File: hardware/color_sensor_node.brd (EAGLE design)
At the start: 27.9 x 27.9 mm, 20 parts, among them J1 JTAG, J2 JTAG, U1 ISL29125, U2 3.3V, U3 WS2811

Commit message: idk
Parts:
- D1: device SparkFun-LED:WS2812B -> SparkFun-LED:WS2812-2020
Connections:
- net 5V: now also D1.4; no longer D1.1
- net DOUT: now also D1.1; no longer D1.2
- net GND: now also D1.2; no longer D1.3
- net N$4: now also D1.3; no longer D1.4
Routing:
- net 5V: track 27.7 -> 31.3 mm
- net DOUT: track 1.54 -> 4.05 mm
- net GND: track 16.5 -> 19.0 mm
- net N$4: track 10.7 -> 12.9 mm
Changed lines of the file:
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@@
 <attribute name="VALUE" x="3.302" y="19.05" size="0.6096" layer="27" font="vector" ratio="20" rot="R90" align="top-center"/>
 </element>
-<element name="D1" library="SparkFun-LED" package="WS2812B" value="WS2812B" x="13.97" y="13.97" rot="R180">
-<attribute name="PROD_ID" value="DIO-12503" x="13.97" y="13.97" size="1.778" layer="27" rot="R180" display="off"/>
-<attribute name="VALUE" value="WS2812B" x="13.97" y="13.97" size="1.778" layer="27" rot="R180" display="off"/>
+<element name="D1" library="SparkFun-LED" package="WS2812-2020" value="WS2812B" x="13.97" y="13.97" rot="R180">
 <attribute name="VALUE" x="13.97" y="16.764" size="0.6096" layer="27" font="vector" ratio="20" rot="R180" align="top-center"/>
 </element>
@@
 <contactref element="U1" pad="3"/>
 <contactref element="U3" pad="4"/>
-<contactref element="D1" pad="3"/>
+<contactref element="D1" pad="2"/>
 <wire x1="7.151" y1="19.05" x2="6.6341" y2="19.05" width="0.4064" layer="1"/>
 <wire x1="8.128" y1="18.2" x2="8.001" y2="18.2" width="0.4064" layer="1"/>
@@
 <via x="19.05" y="11.43" extent="1-16" drill="0.381"/>
 <wire x1="18.33" y1="13.47" x2="16.645" y2="13.47" width="0.2032" layer="1"/>
-<wire x1="16.547" y1="13.372" x2="16.547" y2="12.37" width="0.2032" layer="1"/>
+<wire x1="16.547" y1="13.372" x2="13.055" y2="13.42" width="0.2032" layer="1"/>
 <wire x1="16.645" y1="13.47" x2="16.547" y2="13.372" width="0.2032" layer="1"/>
 <wire x1="19.05" y1="24.13" x2="21.59" y2="26.67" width="0" layer="19" extent="1-1"/>
@@
 <wire x1="18.33" y1="13.47" x2="22.18" y2="16.51" width="0" layer="19" extent="1-16"/>
 <wire x1="19.05" y1="11.43" x2="18.33" y2="13.47" width="0" layer="19" extent="1-1"/>
-<wire x1="13.97" y1="11.43" x2="16.547" y2="12.37" width="0" layer="19" extent="1-1"/>
-<wire x1="16.51" y1="8.89" x2="16.547" y2="12.37" width="0" layer="19" extent="1-1"/>
+<wire x1="13.97" y1="11.43" x2="13.055" y2="13.42" width="0" layer="19" extent="1-1"/>
+<wire x1="16.51" y1="8.89" x2="13.055" y2="13.42" width="0" layer="19" extent="1-1"/>
 <wire x1="24.13" y1="8.89" x2="24.13" y2="13.97" width="0" layer="19" extent="1-1"/>
 <wire x1="26.67" y1="6.35" x2="24.13" y2="8.89" width="0" layer="19" extent="1-1"/>
@@
 <contactref element="U2" pad="3"/>
 <contactref element="C1" pad="1"/>
-<contactref element="D1" pad="1"/>
+<contactref element="D1" pad="4"/>
 <wire x1="8.028" y1="20" x2="6.6341" y2="20" width="0.4064" layer="1"/>
 <wire x1="8.128" y1="19.9" x2="8.028" y2="20" width="0.4064" layer="1"/>
@@
 <wire x1="6.6341" y1="15.9051" x2="6.604" y2="15.875" width="0.4064" layer="1"/>
 <wire x1="6.6341" y1="18.1" x2="6.6341" y2="15.9051" width="0.4064" layer="1"/>
-<wire x1="9.957" y1="15.57" x2="11.393" y2="15.57" width="0.4064" layer="1"/>
+<wire x1="9.957" y1="15.57" x2="14.885" y2="14.52" width="0.4064" layer="1"/>
 <wire x1="9.652" y1="15.875" x2="9.957" y2="15.57" width="0.4064" layer="1"/>
 <contactref element="U3" pad="8"/>
 <via x="5.08" y="5.715" extent="1-16" drill="0.381"/>
 <wire x1="26.08" y1="13.97" x2="22.18" y2="15.24" width="0" layer="19" extent="16-16"/>
-<wire x1="11.393" y1="15.57" x2="22.18" y2="15.24" width="0" layer="19" extent="1-16"/>
+<wire x1="14.885" y1="14.52" x2="22.18" y2="15.24" width="0" layer="19" extent="1-16"/>
 <wire x1="8.3312" y1="15.875" x2="9.652" y2="15.875" width="0" layer="19" extent="1-1"/>
 <wire x1="6.6341" y1="15.9051" x2="8.3312" y2="15.875" width="0" layer="19" extent="1-1"/>
@@
 </signal>
 <signal name="DOUT">
-<contactref element="D1" pad="2"/>
+<contactref element="D1" pad="1"/>
 <contactref element="J2" pad="6"/>
-<wire x1="11.393" y1="10.832" x2="11.393" y2="12.37" width="0.4064" layer="1"/>
+<wire x1="11.393" y1="10.832" x2="13.055" y2="14.52" width="0.4064" layer="1"/>
 <via x="11.393" y="10.832" extent="1-16" drill="0.381"/>
 <wire x1="11.393" y1="10.832" x2="22.18" y2="13.97" width="0" layer="19" extent="1-16"/>
 </signal>
 <signal name="N$4">
-<contactref element="D1" pad="4"/>
+<contactref element="D1" pad="3"/>
 <contactref element="U3" pad="5"/>
 <wire x1="9.398" y1="12.065" x2="8.3312" y2="12.065" width="0.4064" layer="1"/>
 <wire x1="9.779" y1="12.446" x2="9.398" y2="12.065" width="0.4064" layer="1"/>
-<wire x1="16.547" y1="15.57" x2="16.205" y2="15.57" width="0.4064" layer="1"/>
+<wire x1="14.885" y1="13.42" x2="16.205" y2="15.57" width="0.4064" layer="1"/>
 <wire x1="15.24" y1="14.605" x2="10.16" y2="14.605" width="0.4064" layer="1"/>
 <wire x1="10.16" y1="14.605" x2="9.779" y2="14.224" width="0.4064" layer="1"/>

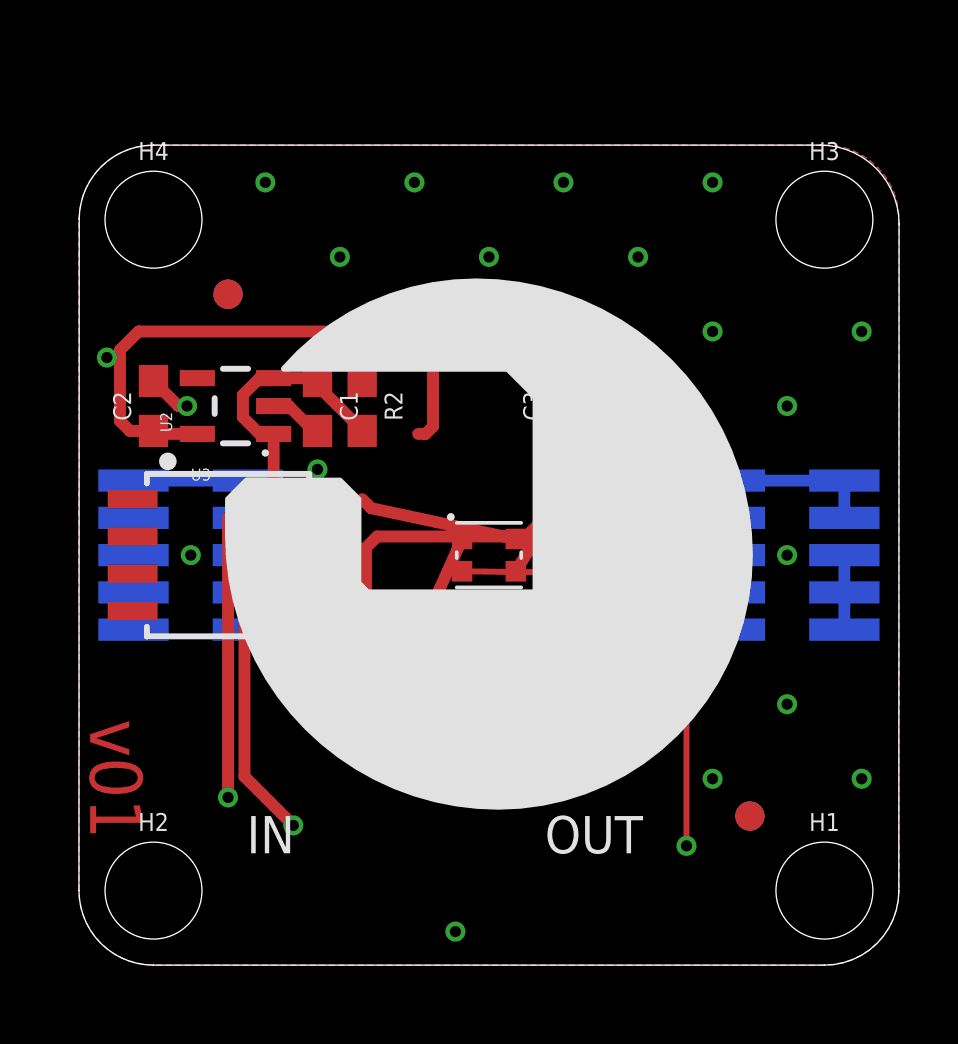
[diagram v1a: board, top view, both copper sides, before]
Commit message: reformat sensor board for hook design
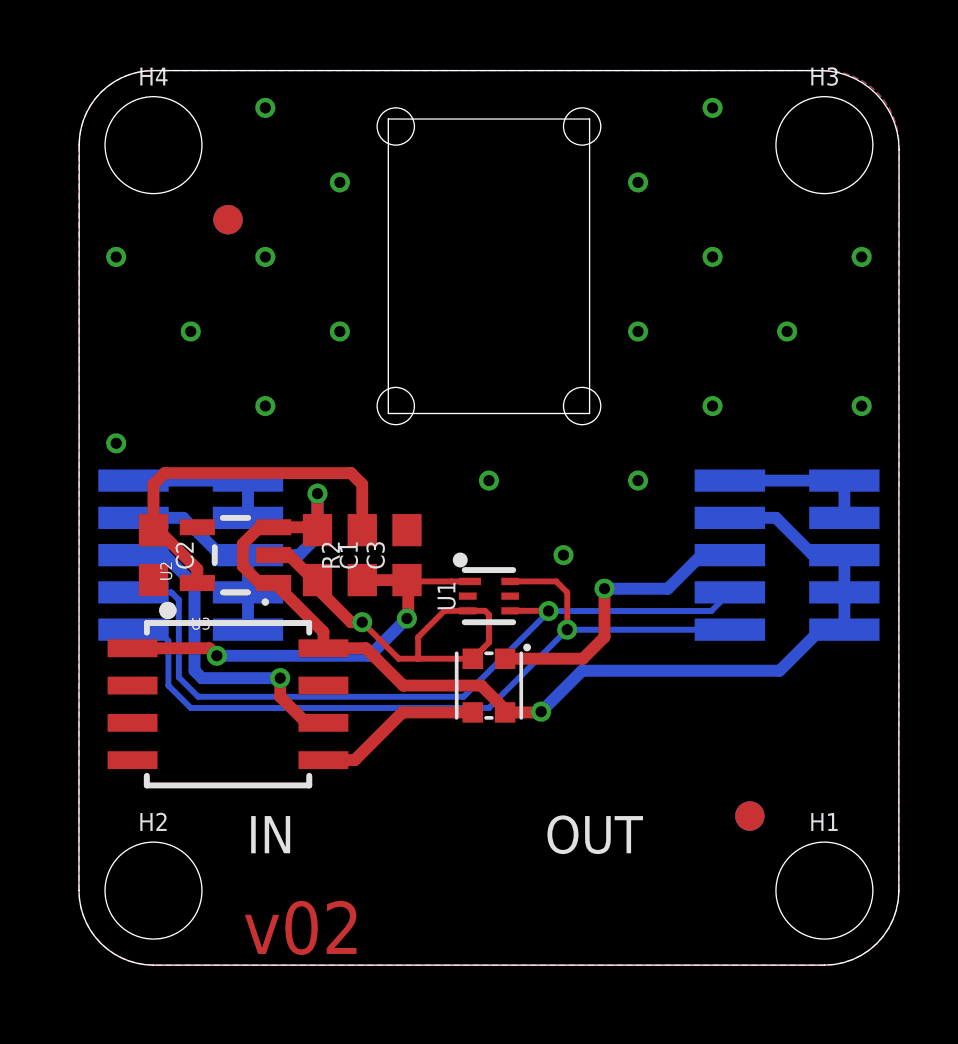
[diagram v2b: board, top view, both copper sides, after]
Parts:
- removed R1: 10k, SparkFun-Resistors:0603
- moved C3 7.37 mm to (11.2, 14.0)
- moved U1 5.27 mm to (14.0, 12.6)
- moved C1 5.08 mm to (8.13, 14.0)
- moved C2 5.08 mm to (2.54, 14.0), turned to 270 degrees
- moved R2 5.08 mm to (9.65, 14.0), turned to 90 degrees
- moved U2 5.08 mm to (5.33, 14.0)
- moved U3 5.08 mm to (5.08, 8.89)
- moved D1 4.45 mm to (14.0, 9.53), turned to 90 degrees
- moved H3 2.54 mm to (25.4, 27.9)
- moved H4 2.54 mm to (2.54, 27.9)
- moved FD1 2.54 mm to (5.08, 25.4)
- moved FD3 2.54 mm to (5.08, 25.4)
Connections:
- removed net N$1: R1.1, U1.5
- net N$2: no longer R1.2
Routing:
- net SDA: track 8.64 -> 26.1 mm
- net 5V: track 31.3 -> 48.1 mm, vias 1 -> 2
- net SCL: track 11.1 -> 26.8 mm
- net N$2: track 5.75 -> 15.0 mm, vias 0 -> 2
- net N$1: track 7.65 -> 0.00 mm
- net N$4: track 12.9 -> 5.76 mm
- net 3.3V: track 19.7 -> 13.1 mm
- net DOUT: track 4.05 -> 10.1 mm
- net GND: track 19.0 -> 24.1 mm, vias 23 -> 20
- net DIN: track 11.7 -> 10.9 mm
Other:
- board size 27.9 x 27.9 mm -> 27.9 x 30.5 mm
- board text added: "v02"
- board text removed: "v01"

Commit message: board designs
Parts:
- moved J1 2.54 mm to (3.81, 11.4)
- moved J2 2.54 mm to (24.1, 11.4)
- moved U3 0.63 mm to (5.71, 8.89)
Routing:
- net 5V: track 48.1 -> 50.9 mm
- net SCL: track 26.8 -> 29.5 mm
- net N$2: track 15.0 -> 17.5 mm
- net SDA: track 26.1 -> 28.6 mm
- net N$4: track 5.76 -> 5.13 mm
- net GND: vias 20 -> 21
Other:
- outline, holes or cut-outs redrawn
- board text added: "v02A"
- board text removed: "v02"
